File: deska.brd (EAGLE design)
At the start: 100 x 80 mm, 18 parts, among them Q1 BC547, Q2 BC547

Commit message: +
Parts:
- moved Q1 53.6 mm to (72.4, 74.9)
- moved BUZZER 52.8 mm to (83.8, 71.1)
- moved R6 25.7 mm to (86.4, 63.5)
- moved NAPAJENI 19.4 mm to (15.2, 5.08), turned to 180 degrees
- moved TIN 15.2 mm to (17.8, 59.7), turned to 0 degrees
- moved TOUT 12.7 mm to (17.8, 41.9), turned to 0 degrees
- moved R4 11.4 mm to (88.9, 53.3), turned to 90 degrees
- moved TUT 7.62 mm to (17.8, 21.6), turned to 0 degrees
- moved R3 6.35 mm to (21.6, 12.7), turned to 180 degrees
- moved R1 6.35 mm to (21.6, 52.1), turned to 180 degrees
- moved I2CKEYB 4.58 mm to (73.7, 27.9), turned to 0 degrees
- moved WEMOS1 3.81 mm to (44.5, 36.8)
- moved R2 3.81 mm to (21.6, 33.0), turned to 180 degrees
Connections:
- net +5V: now also TIN.2, TOUT.2, TUT.2; no longer TIN.1, TOUT.1, TUT.1
- net GND: now also TIN.1, TOUT.1, TUT.1; no longer TIN.3, TOUT.3, TUT.3
- net N$1: now also TIN.3; no longer TIN.2
- net N$19: now also TOUT.3; no longer TOUT.2
- net N$3: now also TUT.3; no longer TUT.2
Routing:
- net +5V: track 0.00 -> 73.7 mm
- net GND: track 0.00 -> 53.3 mm
- net N$3: track 0.00 -> 32.2 mm
- net N$1: track 0.00 -> 27.4 mm
- net N$19: track 0.00 -> 20.5 mm
- net N$11: track 0.00 -> 3.81 mm

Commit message: upravy desky
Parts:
- removed BUZZER, LED, NAPAJENI, RELAY: (no value), con-wago-508:W237-132
- removed I2CDISP, I2CKEYB: (no value), con-wago-508:W237-4P
- removed Q1, Q2: BC547, transistor-npn:TO92
- removed R5, R6: 1k, rcl:0207/7
- removed TIN, TOUT, TUT: (no value), con-wago-508:W237-3E
- added DS18B1, DS18B2, DS18B20, LED+RELAY: (no value), con-wago-508:W237-133
- added PIR, SERIAL: (no value), con-amp-quick:03P
- added SL1: (no value), con-amp-quick:04P
- added SOURCE: (no value), con-wago-508:W237-132
- R1, R3: device rcl:0207/7 -> rcl:0207/10
- R2: value 4k7 -> 220; device rcl:0207/7 -> rcl:0207/10
- R4: value 220 -> 4k7; device rcl:0207/7 -> rcl:0207/10
- WEMOS1: device wemos:WEMOS-D1-MINI -> esp8266modules:WEMOS-D1-MINI
- moved R4 83.6 mm to (10.2, 25.4)
- moved R1 37.0 mm to (7.62, 17.8), turned to 90 degrees
- moved WEMOS1 19.1 mm to (25.4, 35.6)
- moved R3 15.5 mm to (19.1, 27.9), turned to 90 degrees
- moved R2 14.8 mm to (34.3, 25.4), turned to 270 degrees
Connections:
- removed net N$12: I2CDISP.3, I2CKEYB.3, WEMOS1.D4
- removed net N$14: Q2.3, RELAY.1
- removed net N$15: BUZZER.1, Q1.3
- removed net N$16: R6.2, WEMOS1.D2
- removed net N$19: R2.1, TOUT.3, WEMOS1.D5
- new net N$2: SERIAL.3, WEMOS1.RX
- new net N$8: LED+RELAY.3, R2.2
- new net N$9: DS18B20.2, R1.2, WEMOS1.D7
- net +5V: now also DS18B1.3, DS18B2.3, DS18B20.3, LED+RELAY.2, PIR.3, R1.1, R3.1, R4.1, SL1.2, SOURCE.1; no longer I2CDISP.2, I2CKEYB.2, LED.2, NAPAJENI.1, R1.2, R2.2, R3.2, RELAY.2, TIN.2, TOUT.2, TUT.2
- net GND: now also DS18B1.1, DS18B2.1, DS18B20.1, PIR.1, SERIAL.1, SL1.1, SOURCE.2; no longer BUZZER.2, I2CDISP.1, I2CKEYB.1, NAPAJENI.2, Q1.1, Q2.1, TIN.1, TOUT.1, TUT.1
- net N$1: now also SERIAL.2, WEMOS1.TX; no longer R1.1, TIN.3, WEMOS1.D0
- net N$11: now also DS18B2.2, R4.2, WEMOS1.D5; no longer I2CDISP.4, I2CKEYB.4, WEMOS1.D3
- net N$13: now also DS18B1.2, R3.2, WEMOS1.D6; no longer Q2.2, R5.2
- net N$3: now also SL1.4, WEMOS1.D1; no longer R3.1, TUT.3, WEMOS1.D6
- net N$4: now also SL1.3, WEMOS1.D2; no longer R5.1, WEMOS1.D7
- net N$5: now also PIR.2, WEMOS1.D0; no longer R4.1, WEMOS1.D8
- net N$6: now also R2.1, WEMOS1.D4; no longer LED.1, R4.2
- net N$7: now also LED+RELAY.1, WEMOS1.D3; no longer Q1.2, R6.1
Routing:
- net GND: track 53.3 -> 217.4 mm
- net +5V: track 73.7 -> 194.3 mm
- net N$11: track 3.81 -> 56.7 mm
- net N$4: track 0.00 -> 49.5 mm
- net N$13: track 0.00 -> 34.7 mm
- net N$9: track 0.00 -> 31.0 mm
- net N$19: track 20.5 -> 0.00 mm
- net N$1: track 27.4 -> 7.62 mm
- net N$3: track 32.2 -> 49.5 mm
- net N$8: track 0.00 -> 12.6 mm
- net N$5: track 0.00 -> 11.5 mm
- net N$7: track 0.00 -> 11.3 mm
- net N$2: track 0.00 -> 7.62 mm
- net N$6: track 0.00 -> 3.81 mm
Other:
- board size 100 x 80 mm -> 64.4 x 69.8 mm

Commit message: +
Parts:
- moved LED+RELAY 1.27 mm to (48.3, 24.1)
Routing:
- net +5V: track 194.3 -> 201.1 mm
- net GND: track 217.4 -> 220.7 mm
- net N$8: track 12.6 -> 13.9 mm
- net N$11: track 56.7 -> 57.8 mm
- net N$7: track 11.3 -> 11.8 mm
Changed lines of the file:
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@@
 <attribute name="VALUE" x="44.45" y="-1.905" size="1.27" layer="27" ratio="10"/>
 </element>
-<element name="LED+RELAY" library="con-wago-508" package="W237-133" value="" x="46.99" y="24.13" smashed="yes" rot="R270">
-<attribute name="MF" value="" x="46.99" y="24.13" size="1.778" layer="27" rot="R270" display="off"/>
-<attribute name="MPN" value="" x="46.99" y="24.13" size="1.778" layer="27" rot="R270" display="off"/>
-<attribute name="NAME" x="40.132" y="31.115" size="1.27" layer="25" ratio="10" rot="R270"/>
-<attribute name="OC_FARNELL" value="unknown" x="46.99" y="24.13" size="1.778" layer="27" rot="R270" display="off"/>
-<attribute name="OC_NEWARK" value="unknown" x="46.99" y="24.13" size="1.778" layer="27" rot="R270" display="off"/>
-<attribute name="VALUE" x="42.672" y="30.734" size="1.27" layer="27" ratio="10" rot="R270"/>
+<element name="LED+RELAY" library="con-wago-508" package="W237-133" value="" x="48.26" y="24.13" smashed="yes" rot="R270">
+<attribute name="MF" value="" x="48.26" y="24.13" size="1.778" layer="27" rot="R270" display="off"/>
+<attribute name="MPN" value="" x="48.26" y="24.13" size="1.778" layer="27" rot="R270" display="off"/>
+<attribute name="NAME" x="41.402" y="31.115" size="1.27" layer="25" ratio="10" rot="R270"/>
+<attribute name="OC_FARNELL" value="unknown" x="48.26" y="24.13" size="1.778" layer="27" rot="R270" display="off"/>
+<attribute name="OC_NEWARK" value="unknown" x="48.26" y="24.13" size="1.778" layer="27" rot="R270" display="off"/>
+<attribute name="VALUE" x="43.942" y="30.734" size="1.27" layer="27" ratio="10" rot="R270"/>
 </element>
 </elements>
@@
 <contactref element="WEMOS1" pad="GND"/>
 <contactref element="DS18B20" pad="1"/>
-<wire x1="49.53" y1="45.72" x2="49.53" y2="26.67" width="1.016" layer="16"/>
+<wire x1="50.8" y1="45.72" x2="50.8" y2="26.67" width="1.016" layer="16"/>
 <wire x1="2.54" y1="13.97" x2="2.54" y2="29.21" width="1.016" layer="16"/>
-<wire x1="41.91" y1="26.67" x2="49.53" y2="26.67" width="1.016" layer="16"/>
+<wire x1="41.91" y1="26.67" x2="50.8" y2="26.67" width="1.016" layer="16"/>
 <contactref element="PIR" pad="1"/>
 <wire x1="6.35" y1="29.21" x2="2.54" y2="29.21" width="1.016" layer="16"/>
 <contactref element="SERIAL" pad="1"/>
-<wire x1="45.72" y1="45.72" x2="49.53" y2="45.72" width="1.016" layer="16"/>
+<wire x1="45.72" y1="45.72" x2="50.8" y2="45.72" width="1.016" layer="16"/>
 <contactref element="SL1" pad="1"/>
 <wire x1="6.35" y1="38.1" x2="2.54" y2="38.1" width="1.016" layer="16"/>
 <wire x1="2.54" y1="38.1" x2="2.54" y2="29.21" width="1.016" layer="16"/>
 <wire x1="2.54" y1="38.1" x2="2.54" y2="53.34" width="1.016" layer="16"/>
-<wire x1="2.54" y1="53.34" x2="49.53" y2="53.34" width="1.016" layer="16"/>
-<wire x1="49.53" y1="53.34" x2="49.53" y2="45.72" width="1.016" layer="16"/>
+<wire x1="2.54" y1="53.34" x2="50.8" y2="53.34" width="1.016" layer="16"/>
+<wire x1="50.8" y1="53.34" x2="50.8" y2="45.72" width="1.016" layer="16"/>
 <wire x1="40.64" y1="27.94" x2="41.91" y2="26.67" width="1.016" layer="16"/>
 <wire x1="38.1" y1="27.94" x2="40.64" y2="27.94" width="1.016" layer="16"/>
-<contactref element="DS18B2" pad="1"/>
 <contactref element="DS18B1" pad="1"/>
 <wire x1="0" y1="4.445" x2="0" y2="11.43" width="1.016" layer="16"/>
@@
 <wire x1="0" y1="-1.27" x2="15.24" y2="-1.27" width="1.016" layer="16"/>
 <wire x1="15.24" y1="-1.27" x2="15.24" y2="4.445" width="1.016" layer="16"/>
-<wire x1="30.48" y1="4.445" x2="30.48" y2="-1.27" width="1.016" layer="16"/>
-<wire x1="30.48" y1="-1.27" x2="15.24" y2="-1.27" width="1.016" layer="16"/>
+<wire x1="15.24" y1="-1.27" x2="30.48" y2="-1.27" width="1.016" layer="16"/>
 <contactref element="SOURCE" pad="2"/>
-<wire x1="50.8" y1="4.445" x2="50.8" y2="25.4" width="1.016" layer="16"/>
-<wire x1="50.8" y1="25.4" x2="49.53" y2="26.67" width="1.016" layer="16"/>
+<wire x1="50.8" y1="4.445" x2="50.8" y2="26.67" width="1.016" layer="16"/>
+<contactref element="DS18B2" pad="1"/>
+<wire x1="30.48" y1="-1.27" x2="30.48" y2="4.445" width="1.016" layer="16"/>
 </signal>
 <signal name="N$3">
@@
 <wire x1="37.465" y1="1.27" x2="34.29" y2="1.27" width="1.016" layer="16"/>
 <wire x1="34.29" y1="1.27" x2="33.02" y2="2.54" width="1.016" layer="16"/>
-<wire x1="33.02" y1="5.2607875" x2="33.02" y2="2.54" width="1.016" layer="16"/>
-<wire x1="25.4" y1="4.445" x2="28.575" y2="7.62" width="1.016" layer="16"/>
-<wire x1="30.6607875" y1="7.62" x2="33.02" y2="5.2607875" width="1.016" layer="16"/>
-<wire x1="28.575" y1="7.62" x2="30.6607875" y2="7.62" width="1.016" layer="16"/>
+<wire x1="33.02" y1="7.62" x2="33.02" y2="2.54" width="1.016" layer="16"/>
+<wire x1="25.4" y1="4.445" x2="25.4" y2="7.62" width="1.016" layer="16"/>
+<wire x1="25.4" y1="7.62" x2="33.02" y2="7.62" width="1.016" layer="16"/>
 <wire x1="26.67" y1="25.4" x2="26.67" y2="13.97" width="1.016" layer="16"/>
-<wire x1="26.67" y1="13.97" x2="35.56" y2="13.97" width="1.016" layer="16"/>
-<wire x1="35.56" y1="13.97" x2="40.64" y2="8.89" width="1.016" layer="16"/>
-<wire x1="40.64" y1="8.89" x2="40.64" y2="4.445" width="1.016" layer="16"/>
+<wire x1="26.67" y1="13.97" x2="39.37" y2="13.97" width="1.016" layer="16"/>
+<wire x1="39.37" y1="13.97" x2="40.64" y2="12.7" width="1.016" layer="16"/>
+<wire x1="40.64" y1="12.7" x2="40.64" y2="4.445" width="1.016" layer="16"/>
 <wire x1="19.05" y1="22.86" x2="19.05" y2="8.89" width="1.016" layer="16"/>
 <wire x1="19.05" y1="8.89" x2="17.78" y2="7.62" width="1.016" layer="16"/>
@@
 <contactref element="LED+RELAY" pad="2"/>
 <wire x1="38.1" y1="25.4" x2="39.37" y2="24.13" width="1.016" layer="16"/>
-<wire x1="39.37" y1="24.13" x2="46.355" y2="24.13" width="1.016" layer="16"/>
+<wire x1="39.37" y1="24.13" x2="47.625" y2="24.13" width="1.016" layer="16"/>
 </signal>
 <signal name="N$7">
@@
 <contactref element="LED+RELAY" pad="1"/>
 <wire x1="38.1" y1="33.02" x2="45.085" y2="33.02" width="1.016" layer="16"/>
-<wire x1="46.355" y1="31.75" x2="46.355" y2="29.21" width="1.016" layer="16"/>
-<wire x1="46.355" y1="31.75" x2="45.085" y2="33.02" width="1.016" layer="16"/>
+<wire x1="47.625" y1="30.48" x2="47.625" y2="29.21" width="1.016" layer="16"/>
+<wire x1="47.625" y1="30.48" x2="45.085" y2="33.02" width="1.016" layer="16"/>
 </signal>
 <signal name="N$9">
@@
 <signal name="N$11">
 <contactref element="WEMOS1" pad="D5"/>
-<contactref element="DS18B2" pad="2"/>
 <contactref element="R4" pad="2"/>
 <wire x1="24.2316" y1="32.9184" x2="24.2316" y2="10.795" width="1.016" layer="16"/>
@@
 <wire x1="15.24" y1="35.56" x2="21.59" y2="35.56" width="1.016" layer="16"/>
 <wire x1="21.59" y1="35.56" x2="24.2316" y2="32.9184" width="1.016" layer="16"/>
-<wire x1="33.655" y1="10.795" x2="35.56" y2="8.89" width="1.016" layer="16"/>
-<wire x1="35.56" y1="8.89" x2="35.56" y2="4.445" width="1.016" layer="16"/>
-<wire x1="24.2316" y1="10.795" x2="33.655" y2="10.795" width="1.016" layer="16"/>
+<wire x1="24.2316" y1="10.795" x2="35.56" y2="10.795" width="1.016" layer="16"/>
+<contactref element="DS18B2" pad="2"/>
+<wire x1="35.56" y1="4.445" x2="35.56" y2="10.795" width="1.016" layer="16"/>
 </signal>
 <signal name="N$13">
@@
 <contactref element="LED+RELAY" pad="3"/>
 <wire x1="34.29" y1="20.32" x2="35.56" y2="19.05" width="1.016" layer="16"/>
-<wire x1="35.56" y1="19.05" x2="46.355" y2="19.05" width="1.016" layer="16"/>
+<wire x1="35.56" y1="19.05" x2="47.625" y2="19.05" width="1.016" layer="16"/>
 </signal>
 </signals>

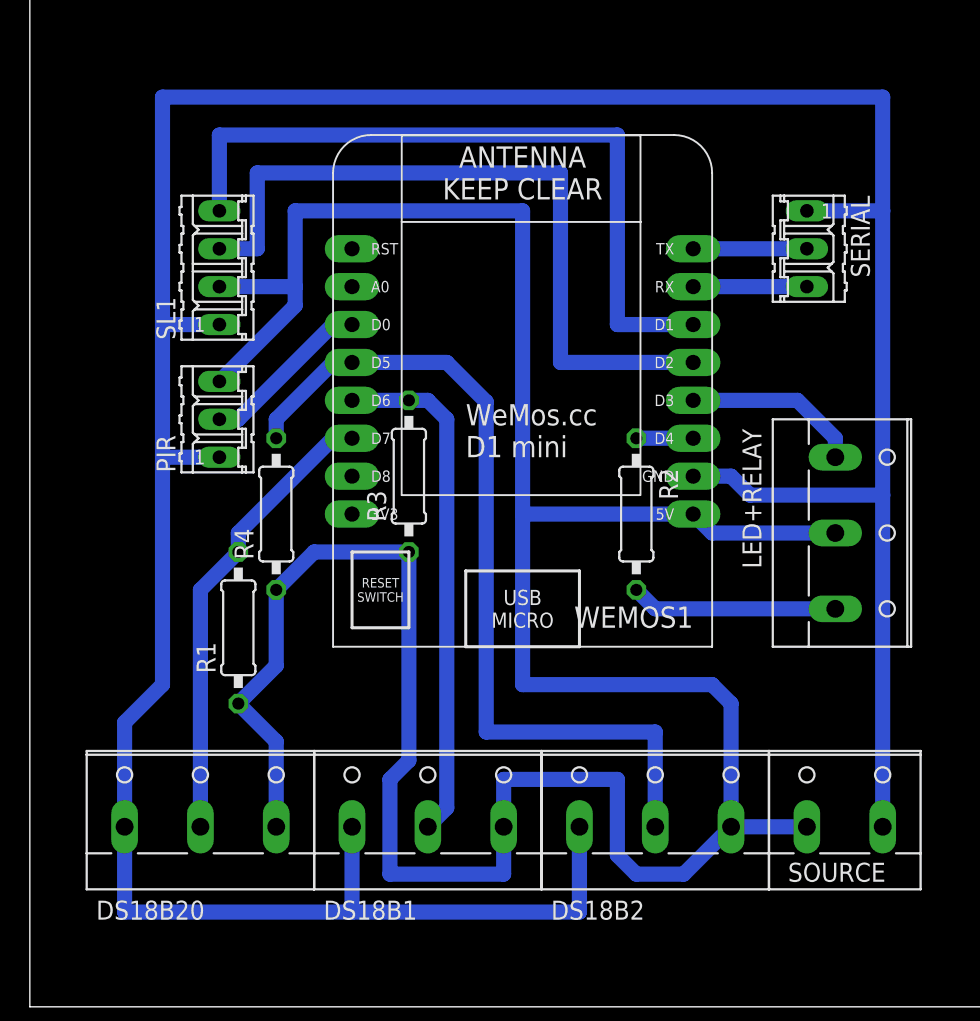
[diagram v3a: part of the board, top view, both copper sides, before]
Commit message: změna na JST XH konektory
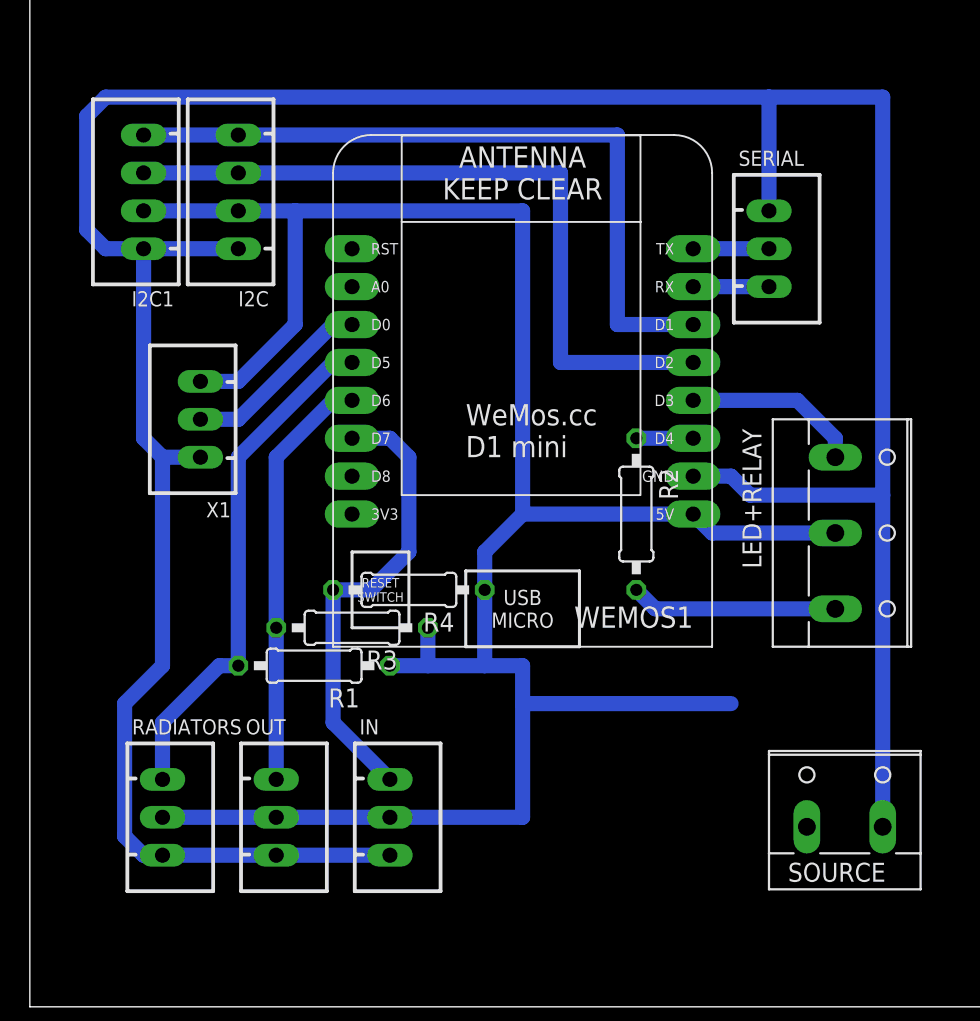
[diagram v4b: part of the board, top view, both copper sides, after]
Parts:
- removed DS18B1, DS18B2, DS18B20: (no value), con-wago-508:W237-133
- removed PIR: (no value), con-amp-quick:03P
- removed SL1: (no value), con-amp-quick:04P
- added I2C, I2C1: JST-XH-04-PIN-LONG-PAD, Rembrandt Electronics - JST XH Connectors v1-0:JST-XH-04-PACKAGE-LONG-PAD
- added IN, OUT, RADIATORS, X1: JST-XH-03-PIN-LONG-PAD, Rembrandt Electronics - JST XH Connectors v1-0:JST-XH-03-PACKAGE-LONG-PAD
- SERIAL: value (none) -> JST-XH-03-PIN-LONG-PAD; device con-amp-quick:03P -> Rembrandt Electronics - JST XH Connectors v1-0:JST-XH-03-PACKAGE-LONG-PAD
- moved R3 10.9 mm to (15.2, 17.8), turned to 180 degrees
- moved R4 10.2 mm to (19.1, 20.3), turned to 180 degrees
- moved R1 5.68 mm to (12.7, 15.2), turned to 180 degrees
- moved SERIAL 2.54 mm to (43.2, 43.2)
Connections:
- net +5V: now also I2C.2, I2C1.2, IN.2, OUT.2, RADIATORS.2, X1.3; no longer DS18B1.3, DS18B2.3, DS18B20.3, PIR.3, SL1.2
- net GND: now also I2C.1, I2C1.1, IN.3, OUT.3, RADIATORS.3, X1.1; no longer DS18B1.1, DS18B2.1, DS18B20.1, PIR.1, SL1.1
- net N$11: now also R1.2, RADIATORS.1; no longer DS18B2.2, R4.2
- net N$13: now also OUT.1; no longer DS18B1.2
- net N$3: now also I2C.4, I2C1.4; no longer SL1.4
- net N$4: now also I2C.3, I2C1.3; no longer SL1.3
- net N$5: now also X1.2; no longer PIR.2
- net N$9: now also IN.1, R4.2; no longer DS18B20.2, R1.2
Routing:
- net +5V: track 201.1 -> 153.7 mm
- net N$11: track 57.8 -> 34.7 mm
- net GND: track 220.7 -> 203.7 mm
- net N$13: track 34.7 -> 28.2 mm
- net N$2: track 7.62 -> 5.08 mm
- net N$1: track 7.62 -> 5.08 mm
- net N$5: track 11.5 -> 12.8 mm

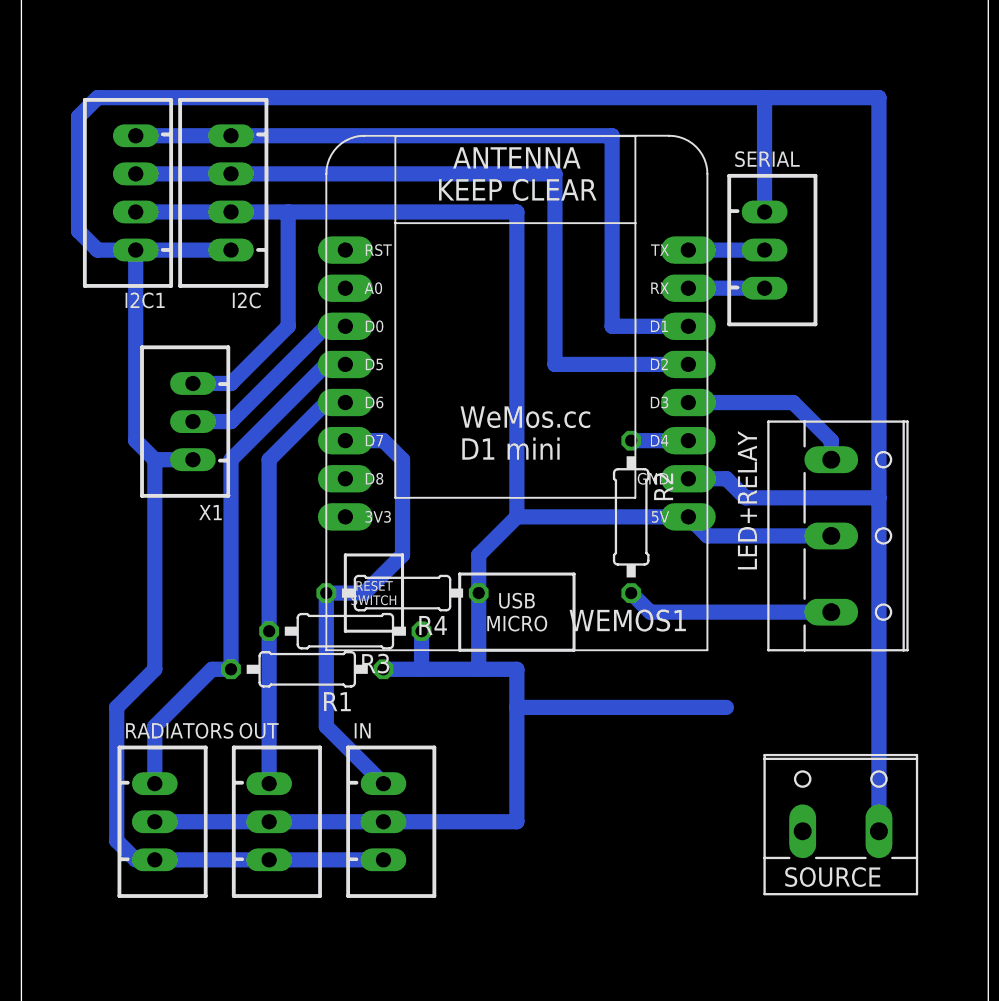
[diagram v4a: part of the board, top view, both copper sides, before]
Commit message: pridana ledka konektory
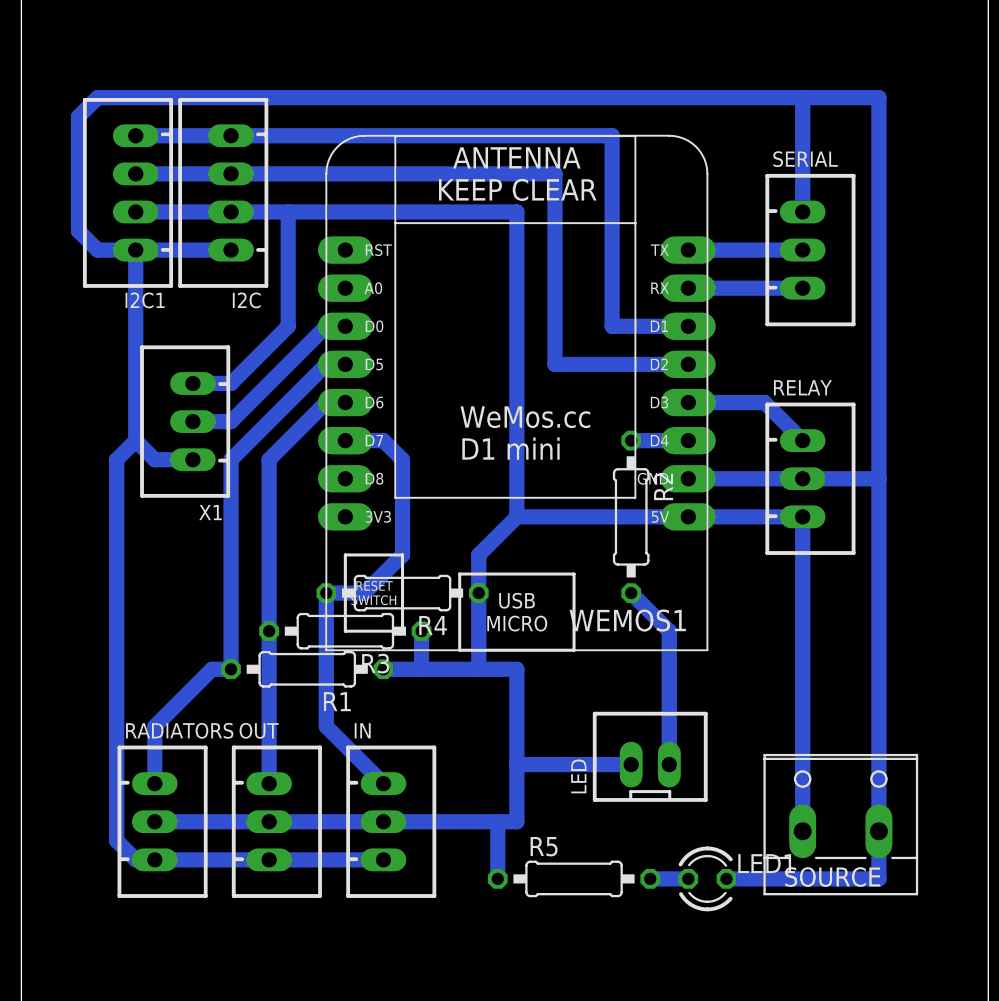
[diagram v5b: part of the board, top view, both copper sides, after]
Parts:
- removed LED+RELAY: (no value), con-wago-508:W237-133
- added LED: JST-XH-02-PIN-LONG-PAD, Rembrandt Electronics - JST XH Connectors v1-0:JST-XH-02-PACKAGE-LONG-PAD
- added LED1: (no value), led:LED3MM
- added R5: 220, rcl:0207/10
- added RELAY: JST-XH-03-PIN-LONG-PAD, Rembrandt Electronics - JST XH Connectors v1-0:JST-XH-03-PACKAGE-LONG-PAD
- moved SERIAL 2.54 mm to (45.7, 43.2)
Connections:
- new net N$10: LED1.A, R5.2
- net +5V: now also LED.1, R5.1, RELAY.3; no longer LED+RELAY.2
- net GND: now also LED1.K, RELAY.2
- net N$7: now also RELAY.1; no longer LED+RELAY.1
- net N$8: now also LED.2; no longer LED+RELAY.3
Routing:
- net +5V: track 153.7 -> 169.6 mm
- net GND: track 203.7 -> 217.3 mm
- net N$7: track 11.8 -> 8.67 mm
- net N$2: track 5.08 -> 7.62 mm
- net N$10: track 0.00 -> 2.54 mm
- net N$1: track 5.08 -> 7.62 mm
- net N$8: track 13.9 -> 12.5 mm
